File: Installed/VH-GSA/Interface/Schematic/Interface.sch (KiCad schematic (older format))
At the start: 30 parts, among them J1 RJ12, J2 RJ12, J3 RJ12, P1 USB_B, P10 CONN_01X03, P11 CONN_01X03, P12 USB_A, P13 USB_A, P14 USB_A, P15 USB_A, P16 USB_A, P17 USB_A, P18 USB_A, P2 USB_B, P3 Anderson 15A, P4 USB_B, P5 USB_B, P6 CONN_01X06, P7 CONN_01X06, P8 CONN_01X06, P9 CONN_01X06, SW1 SW_DPST, U1 MAX232

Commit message: VH-GAS: Added some labels to schematic
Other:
- note added: "12V Supply"
- note added: "Aux"
- note added: "Display / Voice"
- note added: "Flarm Data"
- note added: "Kobo"
- note added: "Operate / Isolate"
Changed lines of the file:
@@
 	7650 2550 5800 2550
 Connection ~ 5800 2550
+Text Notes 6150 600  0    60   ~ 0
+Operate / Isolate
+Text Notes 8700 1400 0    60   ~ 0
+Display / Voice
+Text Notes 8700 2550 0    60   ~ 0
+Flarm Data
+Text Notes 8700 3600 0    60   ~ 0
+Aux
+Text Notes 7250 5000 0    60   ~ 0
+Kobo
+Text Notes 700  6250 0    60   ~ 0
+12V Supply
 $EndSCHEMATC

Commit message: iVH-GSA: Modified schematic  for LXNAV S8
Added connection for LXNAV S8. Modified isolate switch.
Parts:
- removed J1: RJ12, symbol RJ12
- removed SW1: SW_DPST, symbol SW_DPST
- added C? (x15): 1u, symbol CP1_Small
- added C? (x3): 100n, symbol C_Small
- added F? (x3): Polyfuse_Small, symbol Polyfuse_Small
- added J? (x4): RJ45, symbol RJ45
- added J? (x6): RJ12, symbol RJ12
- added P? (x12): CONN_01X06, symbol CONN_01X06
- added P? (x12): USB_B, symbol USB_B
- added P? (x6): CONN_01X03, symbol CONN_01X03
- added P? (x3): Anderson 15A, symbol CONN_01X02
- added P? (x21): USB_A, symbol USB_A
- added SW? (x8): SW_DPDT_x2, symbol SW_DPDT_x2
- added U? (x3): MAX232, symbol MAX232
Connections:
- wire segments 84 -> 344
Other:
- note added: "S8"
- note removed: "Aux"

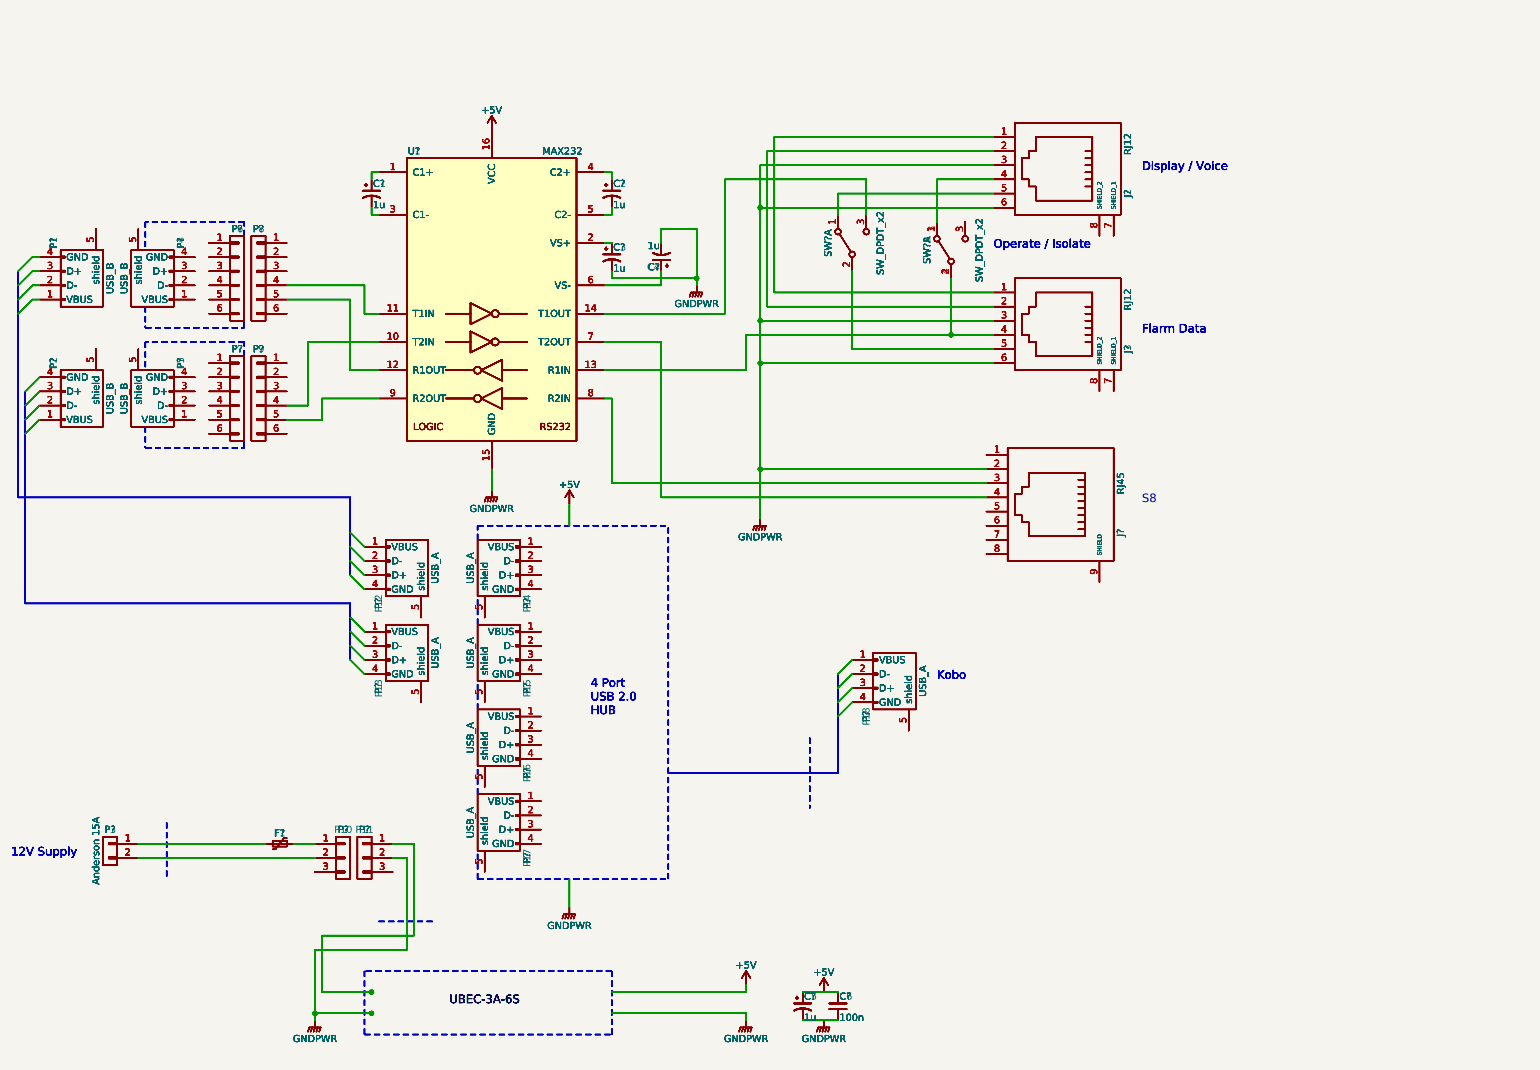
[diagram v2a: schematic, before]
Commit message: VH-GSA: Converted to multi sheet
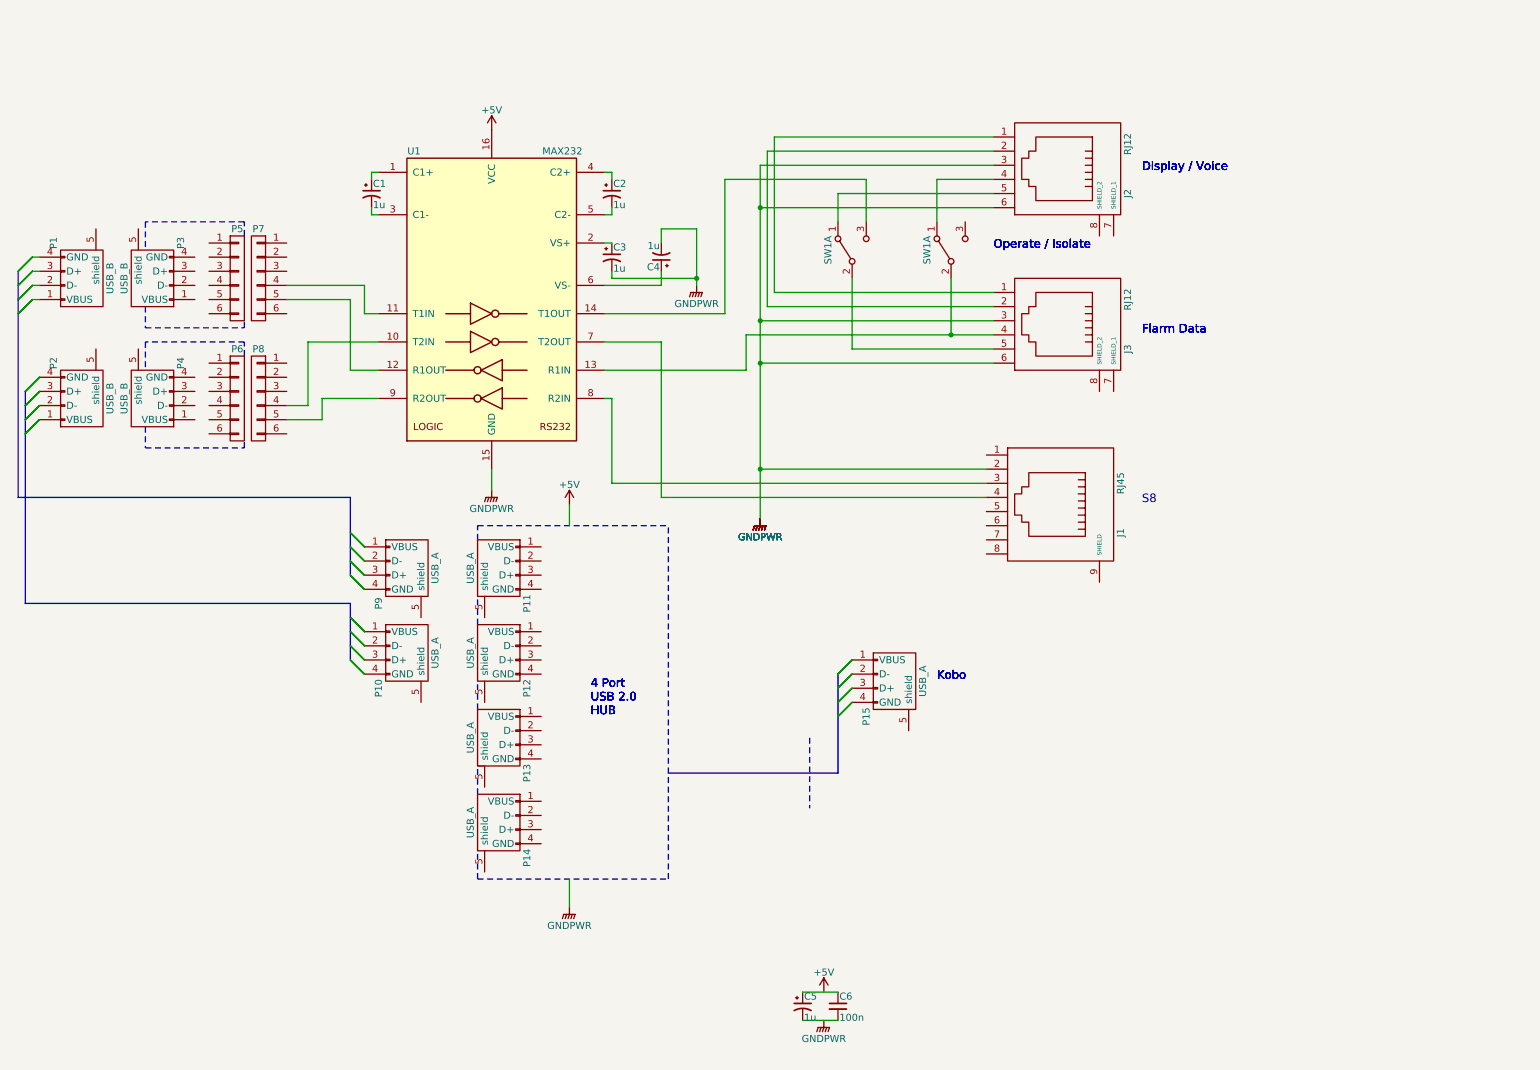
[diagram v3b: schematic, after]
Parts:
- removed C? (x15): 1u, symbol CP1_Small
- removed C? (x3): 100n, symbol C_Small
- removed F1, F? (x3): Polyfuse_Small, symbol Polyfuse_Small
- removed J? (x6): RJ12, symbol RJ12
- removed J? (x3): RJ45, symbol RJ45
- removed P10, P11, P? (x6): CONN_01X03, symbol CONN_01X03
- removed P3, P? (x3): Anderson 15A, symbol CONN_01X02
- removed P? (x12): CONN_01X06, symbol CONN_01X06
- removed P? (x12): USB_B, symbol USB_B
- removed P? (x21): USB_A, symbol USB_A
- removed SW? (x6): SW_DPDT_x2, symbol SW_DPDT_x2
- removed U? (x3): MAX232, symbol MAX232
- gave numbers to parts that had none: 2
- renumbered P13 to P10, P14 to P11, P15 to P12, P16 to P13, P17 to P14, P18 to P15, P4 to P3, P5 to P4, P6 to P5, P7 to P6, P8 to P7, P9 to P8, P12 to P9
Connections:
- net at J3.4, U1.13 (R1IN): now also SW1.2 (B); no longer SW1.4 (B)
- net at J2.4: now also SW1.1 (A); no longer SW1.3 (A)
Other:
- note removed: "12V Supply"
- moved on the sheet: SW1A

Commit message: VH-GSA: Added multiple 5V sources
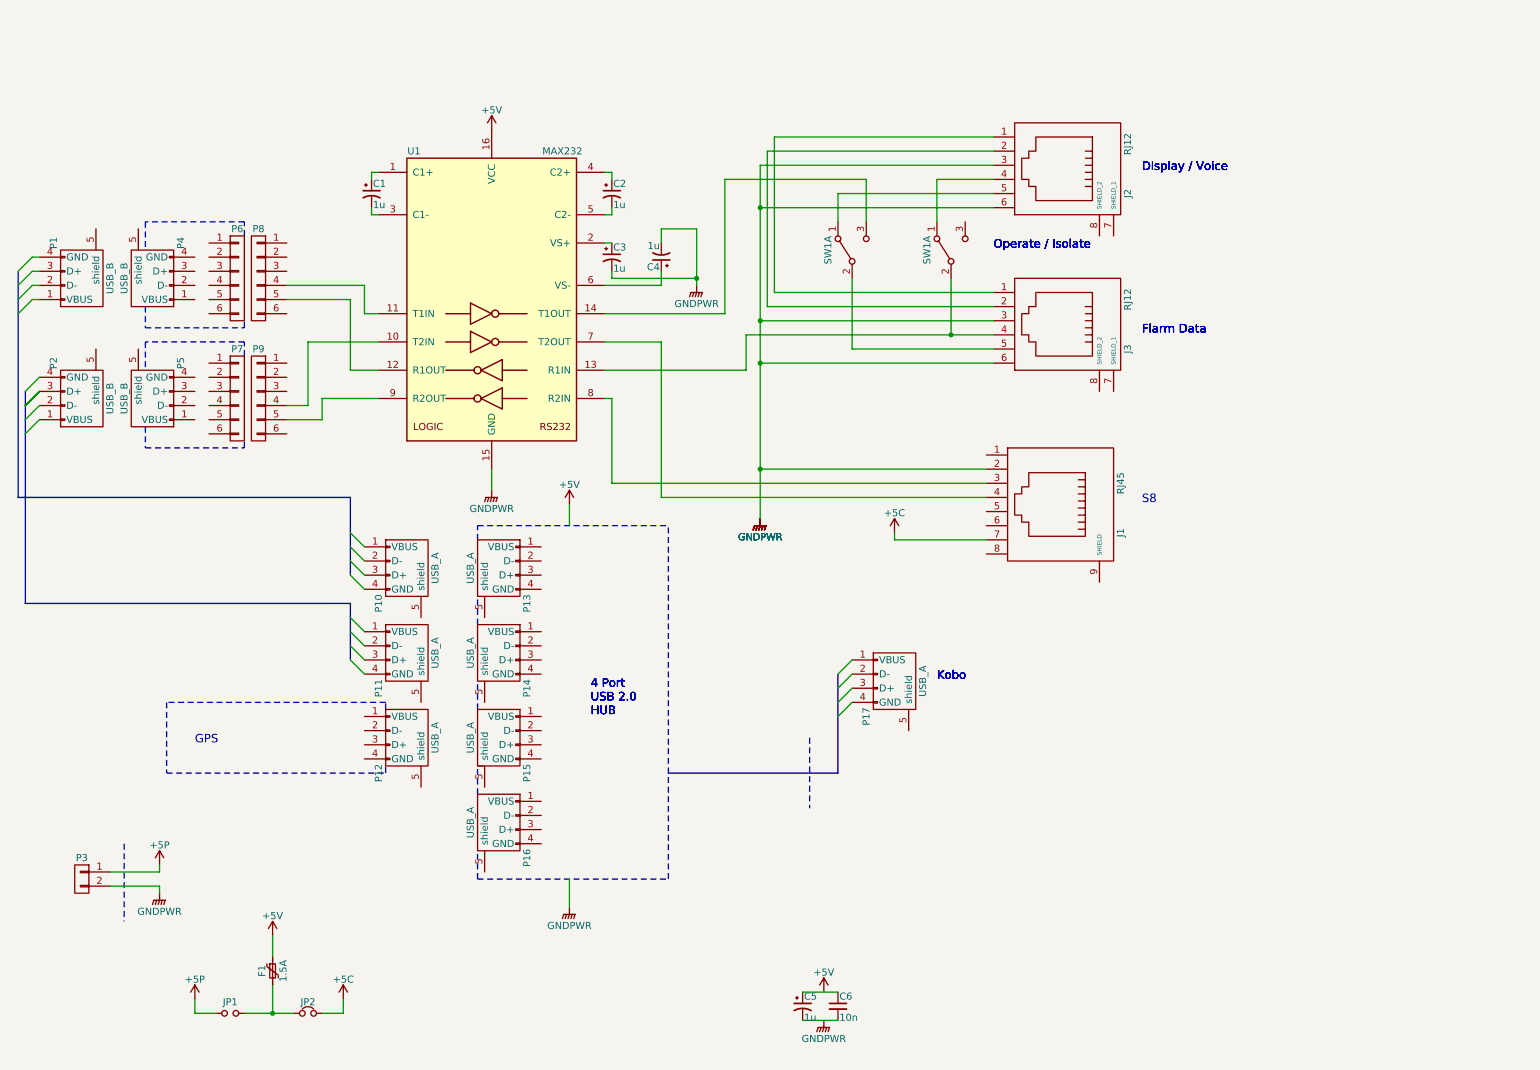
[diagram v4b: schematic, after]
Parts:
- added F1: 1.5A, symbol Polyfuse_Small
- added JP1: Jumper_NO_Small, symbol Jumper_NO_Small
- added JP2: Jumper_NC_Small, symbol Jumper_NC_Small
- added P12: USB_A, symbol USB_A
- added P3: CONN_01X02, symbol CONN_01X02
- C6: value 100n -> 10n
- renumbered P9 to P10, P10 to P11, P11 to P13, P12 to P14, P13 to P15, P14 to P16, P15 to P17, P3 to P4, P4 to P5, P5 to P6, P6 to P7, P7 to P8, P8 to P9
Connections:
- net +5V: now also F1.1
- net GNDPWR: now also P3.2 (P2)
- net +5C: now reaches J1.7
- net +5C: now also JP2.2
- new net: F1.2, JP1.2, JP2.1
- new net +5P: JP1.1, P3.1 (P1)
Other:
- note added: "GPS"

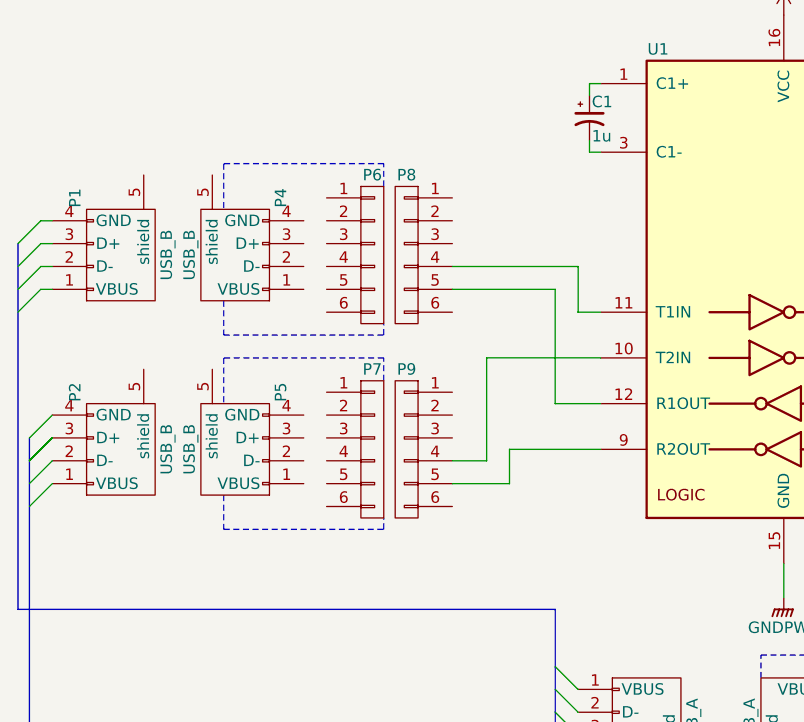
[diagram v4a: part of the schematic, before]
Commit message: VH-GSA: Added GND to FTDI boards
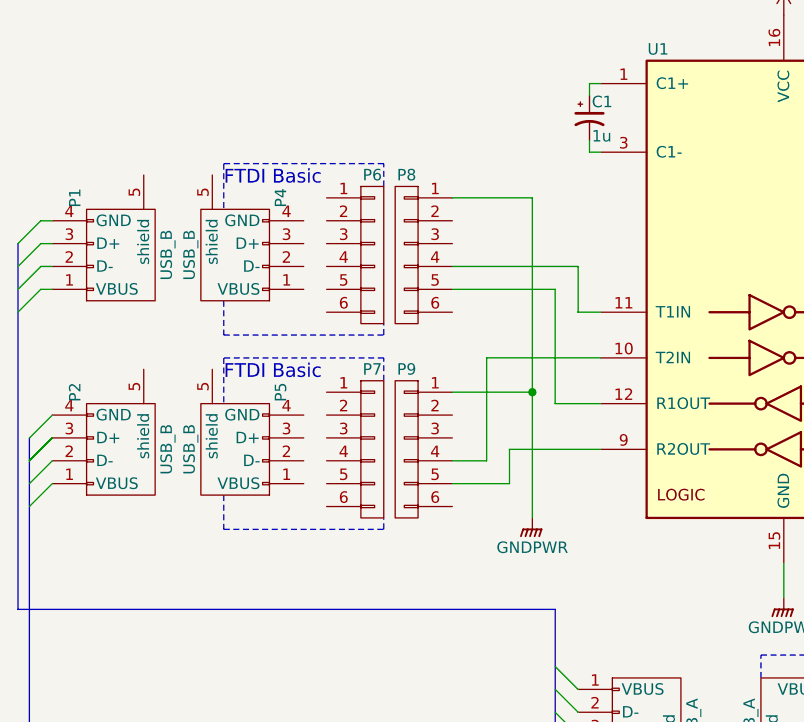
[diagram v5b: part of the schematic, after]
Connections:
- net GNDPWR: now also P8.1 (P1), P9.1 (P1)
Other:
- note added: "FTDI Basic"
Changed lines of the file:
@@
 Wire Notes Line
 	1500 6150 1500 6700
+$Comp
+L GNDPWR #PWR?
+U 1 1 5DB1839A
+P 3000 3300
+F 0 "#PWR?" H 3000 3100 50  0001 C CNN
+F 1 "GNDPWR" H 3000 3170 50  0000 C CNN
+F 2 "" H 3000 3250 50  0000 C CNN
+F 3 "" H 3000 3250 50  0000 C CNN
+	1    3000 3300
+	1    0    0    -1
+$EndComp
+Wire Wire Line
+	2650 1900 3000 1900
+Wire Wire Line
+	3000 1900 3000 3300
+Wire Wire Line
+	2650 2750 3000 2750
+Connection ~ 3000 2750
+Text Notes 1650 1850 0    60   ~ 0
+FTDI Basic
+Text Notes 1650 2700 0    60   ~ 0
+FTDI Basic
 $EndSCHEMATC
